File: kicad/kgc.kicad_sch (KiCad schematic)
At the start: 36 parts, among them IC1 Pico, IC2 MAX7219, IC3 MAX7219

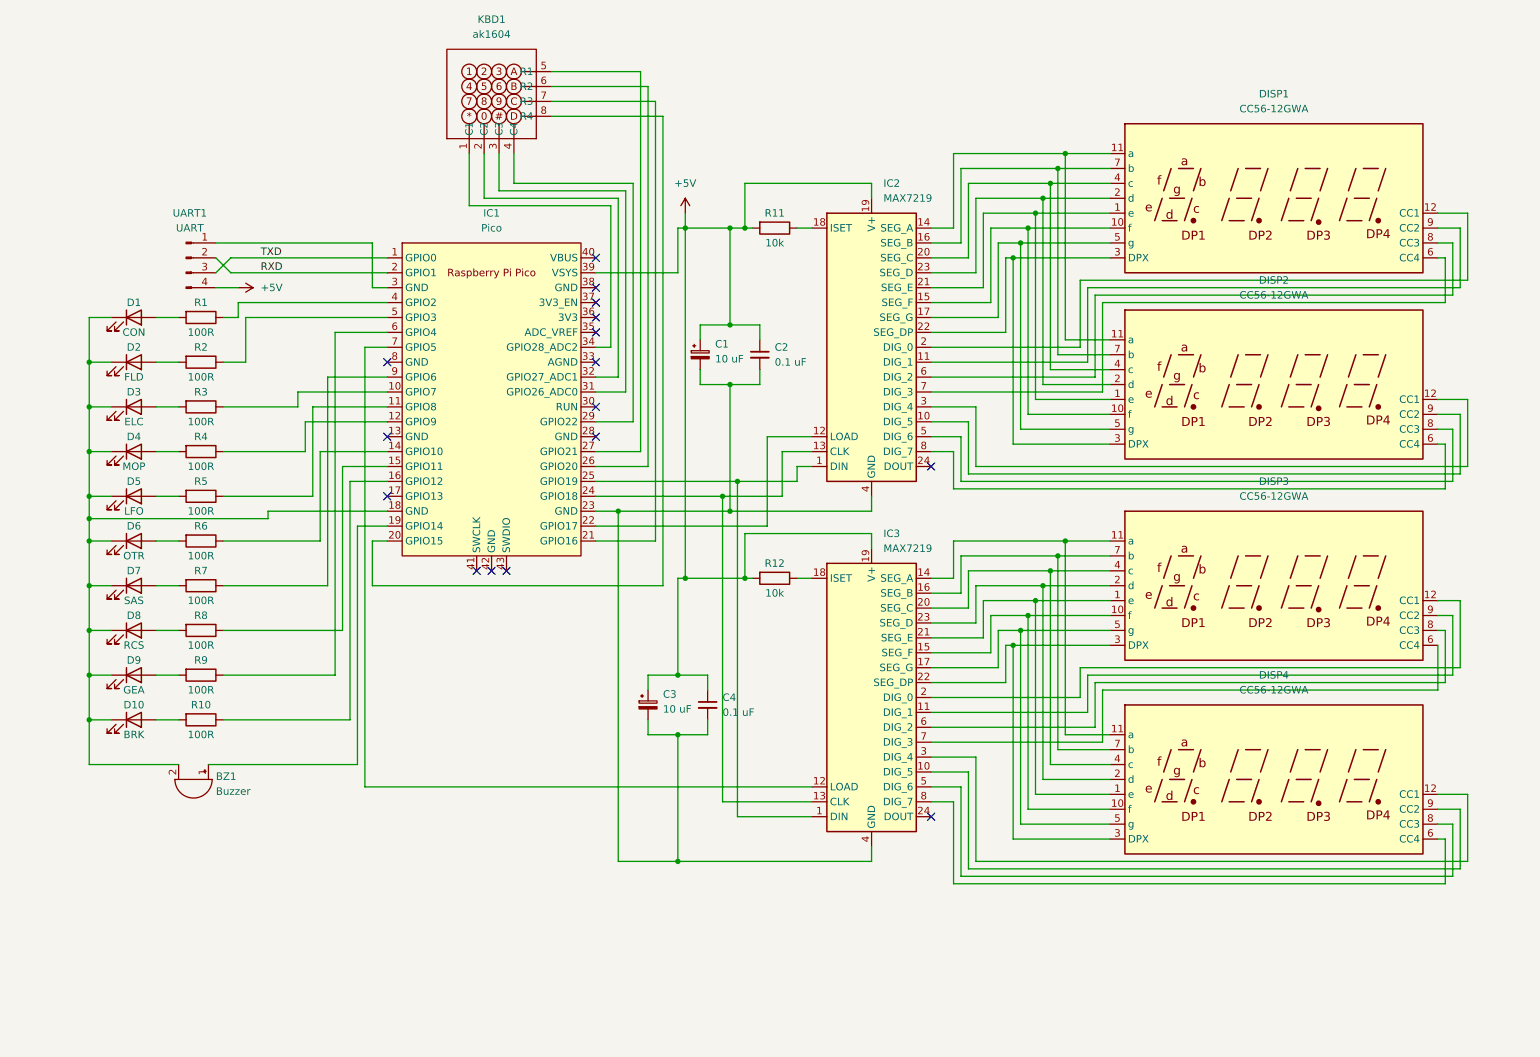
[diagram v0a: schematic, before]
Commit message: New program switching system, support for LED indicators and buzzer, clear_display now clears individual displays, electrical schematic improvements
kgc.c:
  - New macros for LEDs and buzzer GPIO pins.
  - New function led_init for initializing LEDs and buzzer GPIOs.
  - Section and command system was replaced by verb and nouns (yes, I robed it from AGC). Verbs are commands, nouns are relatively independent parameters for verbs (mostly kind of displayed data) . Verbs are executed by core 0 in main, nouns by core1 in core1_entry.
  - Verbs list:
    - 00 for no operation
    - 01 for display data only
    - 99 for device test
  - Nouns list:
    - 00 for no operation
    - 01 for stopwatch
    - 02 for countdown (doesn't work)

keypad.(h/c):
  - Deleted program and prev_program variables.
  - Renamed section and command variables to verb and noun.

max7219.(h/c):
  - Function clear_display now clears individual display, not whole chip.

kicad:
  - Schematic cleanup.
  - PDF version of schematic included.
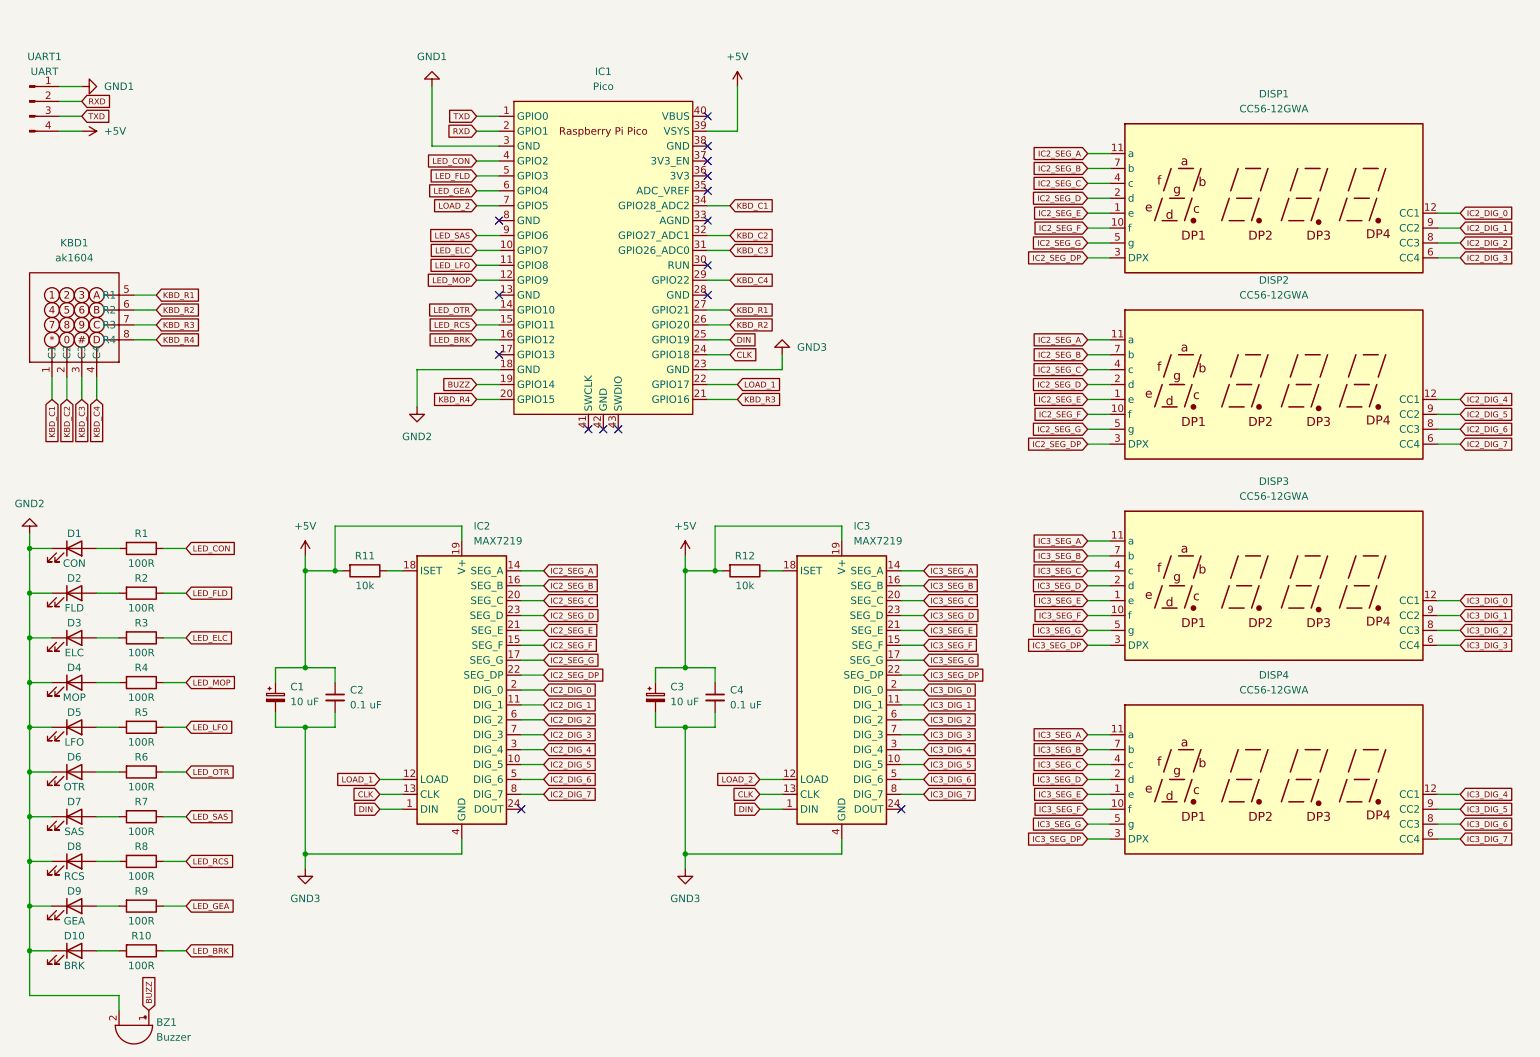
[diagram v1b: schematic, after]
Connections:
- net LED_CON: now reaches IC1.4 (GPIO2), R1.1
- net GND3: now reaches C1.2, C2.2, C3.2, C4.2, IC1.23 (GND), IC2.4 (GND), IC2.9 (GND), IC3.4 (GND), IC3.9 (GND)
- net GND2: now reaches BZ1.2 (+), D1.1 (K), D10.1 (K), D2.1 (K), D3.1 (K), D4.1 (K), D5.1 (K), D6.1 (K), D7.1 (K), D8.1 (K), D9.1 (K), IC1.18 (GND)
- net IC3_SEG_E: now reaches DISP3.1 (e), DISP4.1 (e), IC3.21 (SEG_E)
- net IC3_SEG_F: now reaches DISP3.10 (f), DISP4.10 (f), IC3.15 (SEG_F)
- net IC3_SEG_A: now reaches DISP3.11 (a), DISP4.11 (a), IC3.14 (SEG_A)
- net IC3_DIG_4: now reaches DISP4.12 (CC1), IC3.3 (DIG_4)
- net IC3_SEG_D: now reaches DISP3.2 (d), DISP4.2 (d), IC3.23 (SEG_D)
- net IC3_SEG_DP: now reaches DISP3.3 (DPX), DISP4.3 (DPX), IC3.22 (SEG_DP)
- net IC3_SEG_C: now reaches DISP3.4 (c), DISP4.4 (c), IC3.20 (SEG_C)
- net IC3_SEG_G: now reaches DISP3.5 (g), DISP4.5 (g), IC3.17 (SEG_G)
- net IC3_DIG_7: now reaches DISP4.6 (CC4), IC3.8 (DIG_7)
- net IC3_SEG_B: now reaches DISP3.7 (b), DISP4.7 (b), IC3.16 (SEG_B)
- net IC3_DIG_6: now reaches DISP4.8 (CC3), IC3.5 (DIG_6)
- net IC3_DIG_5: now reaches DISP4.9 (CC2), IC3.10 (DIG_5)
- net IC3_DIG_0: now reaches DISP3.12 (CC1), IC3.2 (DIG_0)
- net IC3_DIG_3: now reaches DISP3.6 (CC4), IC3.7 (DIG_3)
- net IC3_DIG_2: now reaches DISP3.8 (CC3), IC3.6 (DIG_2)
- net IC3_DIG_1: now reaches DISP3.9 (CC2), IC3.11 (DIG_1)
- net LED_LFO: now reaches IC1.11 (GPIO8), R5.1
- net LED_MOP: now reaches IC1.12 (GPIO9), R4.1
- net LED_BRK: now reaches IC1.16 (GPIO12), R10.1
- net LED_FLD: now reaches IC1.5 (GPIO3), R2.1
- net LED_ELC: now reaches IC1.10 (GPIO7), R3.1
- net LED_RCS: now reaches IC1.15 (GPIO11), R8.1
- net DIN: now reaches IC1.25 (GPIO19), IC2.1 (DIN), IC3.1 (DIN)
- net IC2_DIG_5: now reaches DISP2.9 (CC2), IC2.10 (DIG_5)
- net IC2_DIG_1: now reaches DISP1.9 (CC2), IC2.11 (DIG_1)
- net LOAD_1: now reaches IC1.22 (GPIO17), IC2.12 (LOAD)
- net CLK: now reaches IC1.24 (GPIO18), IC2.13 (CLK), IC3.13 (CLK)
- net IC2_SEG_A: now reaches DISP1.11 (a), DISP2.11 (a), IC2.14 (SEG_A)
- net IC2_SEG_F: now reaches DISP1.10 (f), DISP2.10 (f), IC2.15 (SEG_F)
- net IC2_SEG_B: now reaches DISP1.7 (b), DISP2.7 (b), IC2.16 (SEG_B)
- net IC2_SEG_G: now reaches DISP1.5 (g), DISP2.5 (g), IC2.17 (SEG_G)
- net IC2_DIG_0: now reaches DISP1.12 (CC1), IC2.2 (DIG_0)
- net IC2_SEG_C: now reaches DISP1.4 (c), DISP2.4 (c), IC2.20 (SEG_C)
- net IC2_SEG_E: now reaches DISP1.1 (e), DISP2.1 (e), IC2.21 (SEG_E)
- net IC2_SEG_DP: now reaches DISP1.3 (DPX), DISP2.3 (DPX), IC2.22 (SEG_DP)
- net IC2_SEG_D: now reaches DISP1.2 (d), DISP2.2 (d), IC2.23 (SEG_D)
- net IC2_DIG_4: now reaches DISP2.12 (CC1), IC2.3 (DIG_4)
- net IC2_DIG_6: now reaches DISP2.8 (CC3), IC2.5 (DIG_6)
- net IC2_DIG_2: now reaches DISP1.8 (CC3), IC2.6 (DIG_2)
- net IC2_DIG_3: now reaches DISP1.6 (CC4), IC2.7 (DIG_3)
- net IC2_DIG_7: now reaches DISP2.6 (CC4), IC2.8 (DIG_7)
- net BUZZ: now reaches BZ1.1 (-), IC1.19 (GPIO14)
- net LED_GEA: now reaches IC1.6 (GPIO4), R9.1
- net LED_SAS: now reaches IC1.9 (GPIO6), R7.1
- net GND1: now reaches IC1.3 (GND), UART1.1 (Pin_1)
- net LED_OTR: now reaches IC1.14 (GPIO10), R6.1
- net KBD_R4: now reaches IC1.20 (GPIO15), KBD1.8 (R4)
- net KBD_R3: now reaches IC1.21 (GPIO16), KBD1.7 (R3)
- net KBD_R2: now reaches IC1.26 (GPIO20), KBD1.6 (R2)
- net KBD_R1: now reaches IC1.27 (GPIO21), KBD1.5 (R1)
- net KBD_C4: now reaches IC1.29 (GPIO22), KBD1.4 (C4)
- net KBD_C3: now reaches IC1.31 (GPIO26_ADC0), KBD1.3 (C3)
- net KBD_C2: now reaches IC1.32 (GPIO27_ADC1), KBD1.2 (C2)
- net KBD_C1: now reaches IC1.34 (GPIO28_ADC2), KBD1.1 (C1)
- net LOAD_2: now reaches IC1.7 (GPIO5), IC3.12 (LOAD)
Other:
- moved on the sheet: BZ1, C1, C2, C3, C4, D1, D10, D2, D3, D4, D5, D6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

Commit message: New hardware revision
- Created new PCB
- KiCad project updated
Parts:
- removed BZ1: Buzzer, Buzzer_Beeper:Buzzer_12x9.5RM7.6, symbol Device:Buzzer
- removed C1, C3: 10 uF, Capacitor_THT:CP_Radial_D5.0mm_P2.00mm, symbol Device:C_Polarized_Small
- removed C2, C4: 0.1 uF, mistniBordel:C31x, symbol Device:C_Small
- removed D1: CON, LED_THT:LED_D5.0mm, symbol Device:LED
- removed D10: BRK, LED_THT:LED_D5.0mm, symbol Device:LED
- removed D2: FLD, LED_THT:LED_D5.0mm, symbol Device:LED
- removed D3: ELC, LED_THT:LED_D5.0mm, symbol Device:LED
- removed D4: MOP, LED_THT:LED_D5.0mm, symbol Device:LED
- removed D5: LFO, LED_THT:LED_D5.0mm, symbol Device:LED
- removed D6: OTR, LED_THT:LED_D5.0mm, symbol Device:LED
- removed D7: SAS, LED_THT:LED_D5.0mm, symbol Device:LED
- removed D8: RCS, LED_THT:LED_D5.0mm, symbol Device:LED
- removed D9: GEA, LED_THT:LED_D5.0mm, symbol Device:LED
- removed DISP1, DISP2, DISP3, DISP4: CC56-12GWA, Display_7Segment:CC56-12GWA, symbol Display_Character:CC56-12GWA
- removed IC1: Pico, mistniBordel:RPi_Pico_TH, symbol MCU_RaspberryPi_and_Boards:Pico
- removed IC2, IC3: MAX7219, Package_DIP:DIP-24_W7.62mm, symbol Driver_LED:MAX7219
- removed KBD1: ak1604, Connector_PinHeader_2.54mm:PinHeader_1x08_P2.54mm_Vertical, symbol ak1604:ak1604
- removed R10: 100R, Resistor_THT:R_Axial_DIN0207_L6.3mm_D2.5mm_P10.16mm_Horizontal, symbol Device:R
- removed R11, R12: 10k, Resistor_THT:R_Axial_DIN0207_L6.3mm_D2.5mm_P10.16mm_Horizontal, symbol Device:R
- removed UART1: UART, Connector_PinHeader_2.54mm:PinHeader_1x04_P2.54mm_Horizontal, symbol Connector:Conn_01x04_Male
- added C1, C2: 10u, Capacitor_SMD:C_0603_1608Metric_Pad1.08x0.95mm_HandSolder, symbol Device:C
- added C10, C11, C12, C13, C14, C20, C3, C5, C6, C7, C8, C9: 100n, Capacitor_SMD:C_0603_1608Metric_Pad1.08x0.95mm_HandSolder, symbol Device:C
- added C15, C16, C17, C4: 4.7u, Capacitor_SMD:C_0603_1608Metric_Pad1.08x0.95mm_HandSolder, symbol Device:C
- added C18, C19: 15p, Capacitor_SMD:C_0603_1608Metric_Pad1.08x0.95mm_HandSolder, symbol Device:C
- added H1, H2, H3, H4: MountingHole, MountingHole:MountingHole_3.2mm_M3, symbol Mechanical:MountingHole
- added J1: Conn_01x04_Pin, Connector_PinHeader_2.54mm:PinHeader_1x04_P2.54mm_Horizontal, symbol Connector:Conn_01x04_Pin
- added J2: SM03B-SRSS-TB, Connector_JST:JST_SH_SM03B-SRSS-TB_1x03-1MP_P1.00mm_Horizontal, symbol Connector_Generic_MountingPin:Conn_01x03_MountingPin
- added L1: 3.3u, RP2350_80QFN:L_pol_2016, symbol Device:L
- added SW1, SW2: TS6606, Button_Switch_THT:SW_Tactile_SKHH_Angled, symbol Switch:SW_Push
- added TP1, TP2, TP3, TP4, TP5, TP6, TP7, TP8, TP9: TestPoint, TestPoint:TestPoint_Plated_Hole_D2.0mm, symbol Connector:TestPoint
- added U1: NCP1117-3.3_SOT223, Package_TO_SOT_SMD:SOT-223-3_TabPin2, symbol Regulator_Linear:NCP1117-3.3_SOT223
- added U2: RP2350_80QFN, RP2350_80QFN:RP2350-QFN-80-1EP_10x10_P0.4mm_EP3.4x3.4mm_ThermalVias, symbol MCU_RaspberryPi_RP2350:RP2350_80QFN
- added U3: W25Q128JVS, Package_SO:SOIC-8_5.3x5.3mm_P1.27mm, symbol Memory_Flash:W25Q128JVS
- added Y1: ABM8-272-T3, Crystal:Crystal_SMD_3225-4Pin_3.2x2.5mm, symbol Device:Crystal_GND24
- R1: value 100R -> 33; footprint Resistor_THT:R_Axial_DIN0207_L6.3mm_D2.5mm_P10.16mm_Horizontal -> Resistor_SMD:R_0603_1608Metric_Pad0.98x0.95mm_HandSolder
- R2, R3: value 100R -> 27R; footprint Resistor_THT:R_Axial_DIN0207_L6.3mm_D2.5mm_P10.16mm_Horizontal -> Resistor_SMD:R_0603_1608Metric_Pad0.98x0.95mm_HandSolder
- R4, R5, R6: value 100R -> 1k; footprint Resistor_THT:R_Axial_DIN0207_L6.3mm_D2.5mm_P10.16mm_Horizontal -> Resistor_SMD:R_0603_1608Metric_Pad0.98x0.95mm_HandSolder
- R7, R8: value 100R -> DNF; footprint Resistor_THT:R_Axial_DIN0207_L6.3mm_D2.5mm_P10.16mm_Horizontal -> Resistor_SMD:R_0603_1608Metric_Pad0.98x0.95mm_HandSolder
- R9: value 100R -> 0R; footprint Resistor_THT:R_Axial_DIN0207_L6.3mm_D2.5mm_P10.16mm_Horizontal -> Resistor_SMD:R_0603_1608Metric_Pad0.98x0.95mm_HandSolder
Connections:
- net BUZZ: now also U2.58 (GPIO47_ADC7)
- net LED_BRK: now also U2.20 (GPIO20)
- net LED_CON: now also U2.53 (GPIO42_ADC2); no longer R1.1
- net LED_ELC: now also U2.43 (GPIO34); no longer R3.1
- net LED_FLD: now also U2.16 (GPIO16); no longer R2.1
- net LED_GEA: now also U2.47 (GPIO38); no longer R9.1
- net LED_LFO: now also U2.49 (GPIO40_ADC0); no longer R5.1
- net LED_MOP: now also U2.17 (GPIO17); no longer R4.1
- net LED_OTR: now also U2.18 (GPIO18); no longer R6.1
- net LED_RCS: now also U2.19 (GPIO19); no longer R8.1
- net LED_SAS: now also U2.48 (GPIO39); no longer R7.1
- net at R1.2: now also C15.1, U2.61 (VREG_AVDD)
- net USB D+: now reaches R2.2
- net at R5.2: now also U2.35 (RUN)
- net QSPI_SS: now reaches R4.2
- net QSPI_SS: now also R9.1, U2.75 (QSPI_SS)
- net USB D-: now reaches R3.2
- net FLASH_SS: now reaches R8.2
- net FLASH_SS: now also R7.2, R9.2, U3.1 (~{CS})
- net at R6.2: now also C19.1, Y1.3
- new net: R4.1, SW1.2
- new net: R5.1, SW2.2
- new net: L1.2, U2.63 (VREG_LX)
- new net: R3.1, U2.66 (USB_DM)
- new net: R2.1, U2.67 (USB_DP)
- new net +1V1: C17.1, C3.1, C4.1, C5.1, L1.1, U2.10 (DVDD), U2.32 (DVDD), U2.51 (DVDD), U2.65 (VREG_FB)
- new net +3V3: C10.1, C11.1, C12.1, C13.1, C14.1, C16.1, C2.1, C20.1, C6.1, C7.1, C8.1, C9.1, J1.4 (Pin_4), R1.1, R8.1, U1.2 (VO), U2.15 (IOVDD), U2.24 (IOVDD), U2.29 (IOVDD), U2.41 (IOVDD), U2.5 (IOVDD), U2.50 (IOVDD), U2.59 (ADC_AVDD), U2.60 (IOVDD), U2.64 (VREG_VIN), U2.68 (USB_OTP_VDD), U2.69 (QSPI_IOVDD), U2.76 (IOVDD), U3.8 (VCC)
- new net GND: C1.2, C10.2, C11.2, C12.2, C13.2, C14.2, C15.2, C16.2, C17.2, C18.2, C19.2, C2.2, C20.2, C3.2, C4.2, C5.2, C6.2, C7.2, C8.2, C9.2, J1.1 (Pin_1), J2.2 (Pin_2), J2.MP (MountPin), SW1.1, SW2.1, U1.1 (GND), U2.62 (VREG_PGND), U2.81 (GND), U3.4 (GND), Y1.2, Y1.4
- new net KBD_COL_1: U2.36 (GPIO28)
- new net KBD_COL_2: U2.28 (GPIO27)
- new net KBD_COL_3: U2.27 (GPIO26)
- new net KBD_COL_4: U2.25 (GPIO24)
- new net KBD_COL_5: U2.23 (GPIO23)
- new net KBD_COL_6: U2.22 (GPIO22)
- new net KBD_COL_7: U2.21 (GPIO21)
- new net KBD_ROW_1: U2.37 (GPIO29)
- new net KBD_ROW_2: U2.38 (GPIO30)
- new net KBD_ROW_3: U2.39 (GPIO31)
- new net QSPI_SCLK: U2.71 (QSPI_SCLK), U3.6 (CLK)
- new net QSPI_SD0: U2.72 (QSPI_SD0), U3.5 (DI/IO_{0})
- new net QSPI_SD1: U2.74 (QSPI_SD1), U3.2 (DO/IO_{1})
- new net QSPI_SD2: U2.73 (QSPI_SD2), U3.3 (~{WP}/IO_{2})
- new net QSPI_SD3: U2.70 (QSPI_SD3), U3.7 (~{HOLD}/~{RESET}/IO_{3})
- new net SPI1_MOSI: TP9.1, U2.9 (GPIO11)
- new net SPI1_SCK: TP7.1, U2.8 (GPIO10)
- new net SWCLK: J2.1 (Pin_1), U2.33 (SWCLK)
- new net SWD: J2.3 (Pin_3), U2.34 (SWD)
- new net UART0_RX: J1.3 (Pin_3), U2.78 (GPIO1)
- new net UART0_TX: J1.2 (Pin_2), R7.1, U2.77 (GPIO0)
- new net UART1_CTS: TP6.1, U2.4 (GPIO7)
- new net UART1_RTS: TP8.1, U2.3 (GPIO6)
- new net UART1_RX: TP2.1, U2.2 (GPIO5)
- new net UART1_TX: TP4.1, U2.1 (GPIO4)
- new net VBUS: C1.1, U1.3 (VI)
- new net XIN: C18.1, U2.30 (XIN), Y1.1
- new net XOUT: R6.1, U2.31 (XOUT)
- new net ~{SPI1_SS1}: TP1.1, U2.26 (GPIO25)
- new net ~{SPI1_SS2}: TP3.1, U2.12 (GPIO13)
- new net ~{SPI1_SS3}: TP5.1, U2.7 (GPIO9)
- no-connect marks 16 -> 17
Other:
- added sheet Displays and LEDs (displays_leds.kicad_sch)
- added sheet Keyboard (keyboard.kicad_sch)
- added sheet USB (usb.kicad_sch)
- note added: "12MHz Crystal"
- note added: "Debug"
- note added: "Flash"
- note added: "MCU"
- note added: "Power"
